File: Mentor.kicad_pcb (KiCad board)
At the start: 2 copper layers, 50 x 100 mm, 41 parts, among them J1 CONN_01X02, J2 CONN_01X06, J3 CONN_01X09, J4 CONN_01X10, J5 CONN_01X02, J6 CONN_01X03, J7 CONN_01X09, Q1 PZT2222A, Q2 PZT2222A, Q3 IRFR3303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

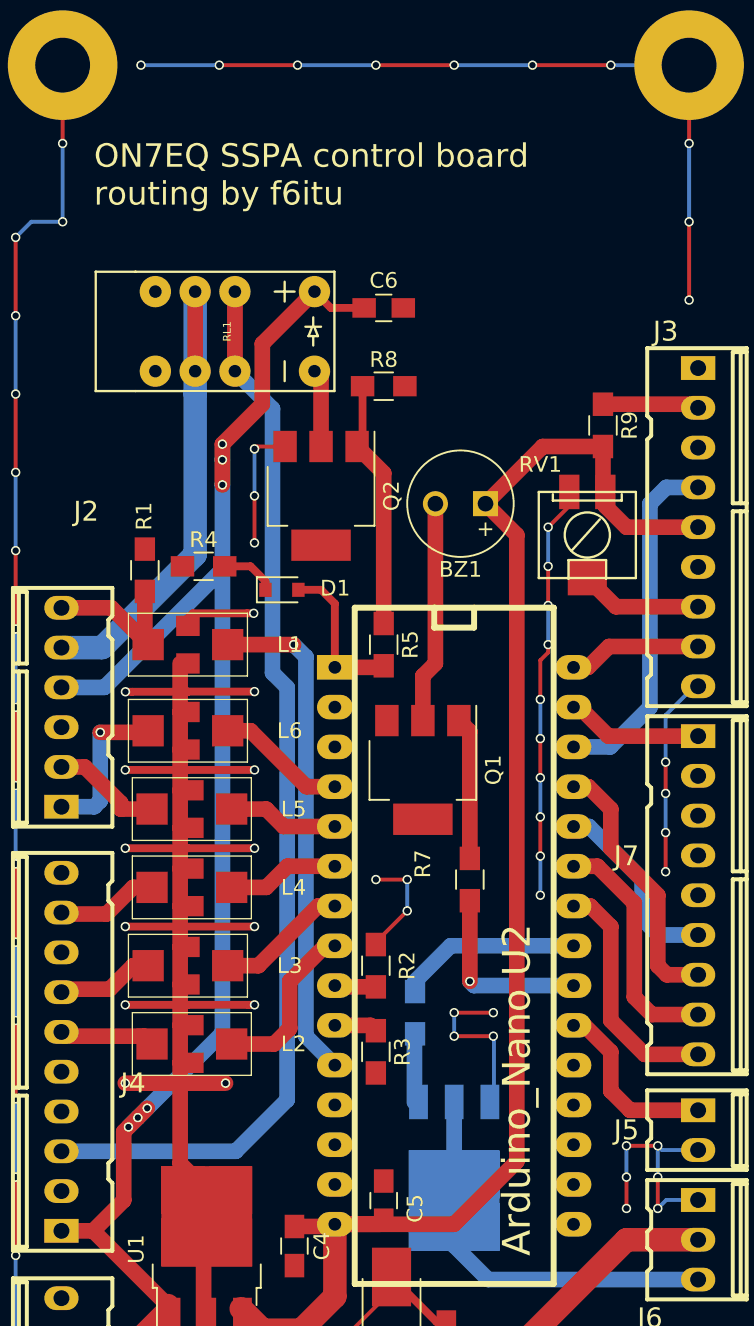
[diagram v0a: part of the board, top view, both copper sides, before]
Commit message: buzzer changed
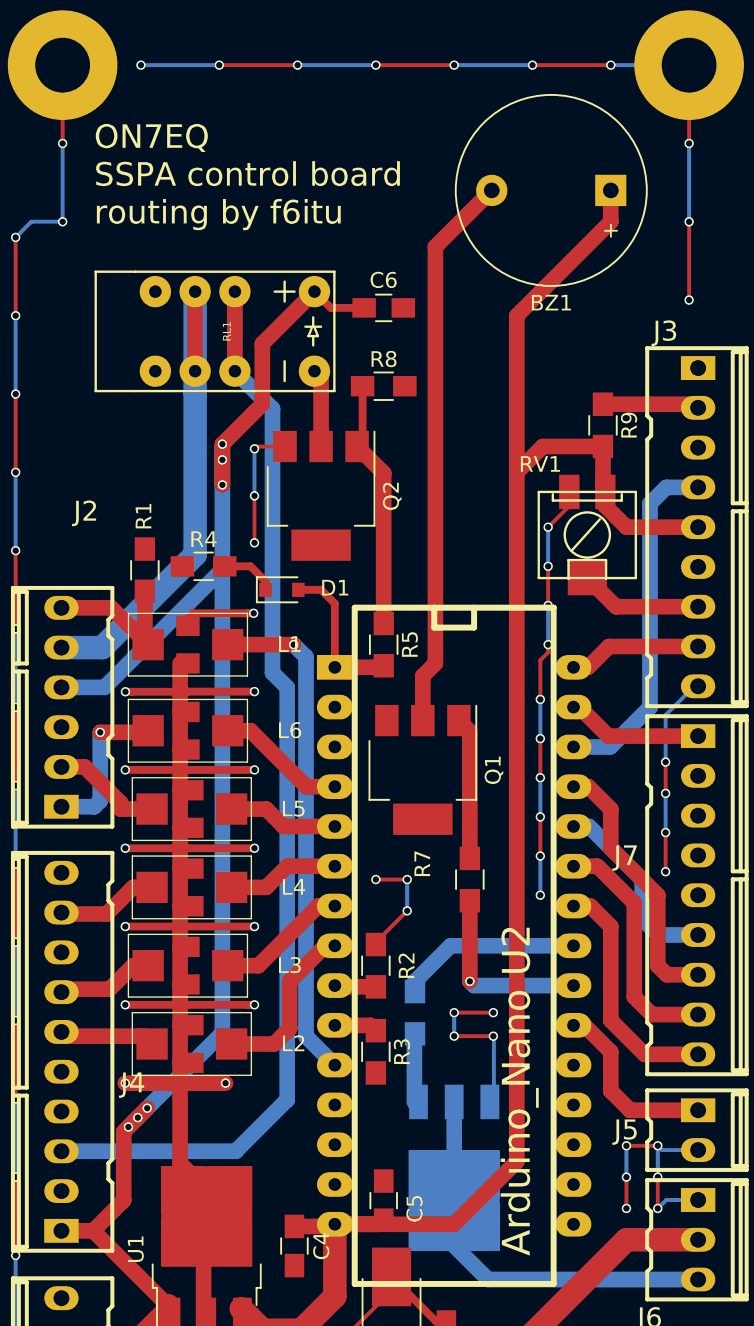
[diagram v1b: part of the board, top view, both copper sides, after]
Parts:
- BZ1: footprint Buzzers_Beepers:MagneticBuzzer_Kingstate_KCG0601 -> Buzzers_Beepers:Buzzer_12x9.5RM7.6
- R4: value R -> 330
- moved BZ1 21.5 mm to (200.0, 48.0)
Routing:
- net Net-(BZ1-Pad2): track 14.2 -> 35.7 mm
- net +5V: track 93.9 -> 112.8 mm
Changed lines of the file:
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@@
     (links 112)
     (no_connects 0)
-    (area 148.5808 34.525 219.0716 135.575)
+    (area 159.924999 34.924999 210.075001 135.075001)
     (thickness 1.6)
     (drawings 13)
-    (tracks 430)
+    (tracks 433)
     (zones 0)
     (modules 41)
@@
   )
   (setup
-    (last_trace_width 0.25)
+    (last_trace_width 1)
     (user_trace_width 0.5)
     (user_trace_width 1)
@@
     )
   )
-  (module Buzzers_Beepers:MagneticBuzzer_Kingstate_KCG0601 (layer F.Cu)
-    (at 192 68 180)
-    (descr "Buzzer, Elektromagnetic Beeper, Summer,")
-    (tags "Kingstate KCG0601 ")
-    (fp_text reference BZ1 (at 1.6 -4.2 180) (layer F.SilkS)
-      (effects (font (size 1 1) (thickness 0.15)))
-    )
-    (fp_text value Buzzer (at 1.6 4.4 180) (layer F.Fab)
-      (effects (font (size 1 1) (thickness 0.15)))
-    )
-    (fp_text user + (at 0 -1.6 180) (layer F.SilkS)
-      (effects (font (size 1 1) (thickness 0.15)))
-    )
-    (fp_text user + (at 0 -1.6 180) (layer F.Fab)
-      (effects (font (size 1 1) (thickness 0.15)))
-    )
-    (fp_circle (center 1.6 0) (end 5.15 0) (layer F.CrtYd) (width 0.05))
-    (fp_circle (center 1.6 0) (end 4.9 0) (layer F.Fab) (width 0.1))
-    (fp_circle (center 1.6 0) (end 2.4 0) (layer F.Fab) (width 0.1))
-    (fp_text user %R (at 1.6 -4.2 180) (layer F.Fab)
-      (effects (font (size 1 1) (thickness 0.15)))
-    )
-    (fp_circle (center 1.6 0) (end 5 0) (layer F.SilkS) (width 0.12))
-    (pad 1 thru_hole rect (at 0 0 180) (size 1.6 1.6) (drill 1) (layers *.Cu *.Mask)
-      (net 1 +5V))
-    (pad 2 thru_hole circle (at 3.2 0 180) (size 1.6 1.6) (drill 1) (layers *.Cu *.Mask)
-      (net 2 "Net-(BZ1-Pad2)"))
-    (model Buzzers_Beepers.3dshapes/MagneticBuzzer_Kingstate_KCG0601.wrl
-      (at (xyz 0.1248031496062992 0 0))
-      (scale (xyz 1 1 1))
-      (rotate (xyz 0 0 180))
-    )
-  )
   (module Capacitors_SMD:C_0805_HandSoldering (layer F.Cu)
     (at 170.8 124.8 180)
@@
       (effects (font (size 1 1) (thickness 0.15)))
     )
-    (fp_text value R (at 0 1.75) (layer F.Fab)
+    (fp_text value 330 (at 0 1.75) (layer F.Fab)
       (effects (font (size 1 1) (thickness 0.15)))
     )
@@
     )
   )
-  (gr_text "ON7EQ SSPA control board\nrouting by f6itu" (at 167 47) (layer F.SilkS)
+  (module Buzzers_Beepers:Buzzer_12x9.5RM7.6 (layer F.Cu)
+    (at 200 48 180)
+    (descr "Generic Buzzer, D12mm height 9.5mm with RM7.6mm")
+    (tags buzzer)
+    (fp_text reference BZ1 (at 3.8 -7.2 180) (layer F.SilkS)
+      (effects (font (size 1 1) (thickness 0.15)))
+    )
+    (fp_text value Buzzer (at 3.8 7.4 180) (layer F.Fab)
+      (effects (font (size 1 1) (thickness 0.15)))
+    )
+    (fp_text user + (at -0.01 -2.54 180) (layer F.Fab)
+      (effects (font (size 1 1) (thickness 0.15)))
+    )
+    (fp_text user + (at -0.01 -2.54 180) (layer F.SilkS)
+      (effects (font (size 1 1) (thickness 0.15)))
+    )
+    (fp_text user %R (at 3.8 -4 180) (layer F.Fab)
+      (effects (font (size 1 1) (thickness 0.15)))
+    )
+    (fp_circle (center 3.8 0) (end 10.05 0) (layer F.CrtYd) (width 0.05))
+    (fp_circle (center 3.8 0) (end 9.8 0) (layer F.Fab) (width 0.1))
+    (fp_circle (center 3.8 0) (end 4.8 0) (layer F.Fab) (width 0.1))
+    (fp_circle (center 3.8 0) (end 9.9 0) (layer F.SilkS) (width 0.12))
+    (pad 1 thru_hole rect (at 0 0 180) (size 2 2) (drill 1) (layers *.Cu *.Mask)
+      (net 1 +5V))
+    (pad 2 thru_hole circle (at 7.6 0 180) (size 2 2) (drill 1) (layers *.Cu *.Mask)
+      (net 2 "Net-(BZ1-Pad2)"))
+    (model ${KISYS3DMOD}/Buzzers_Beepers.3dshapes/Buzzer_12x9.5RM7.6.wrl
+      (at (xyz 0.15 0 0))
+      (scale (xyz 4 4 4))
+      (rotate (xyz 0 0 0))
+    )
+  )
+  (gr_text "ON7EQ \nSSPA control board\nrouting by f6itu" (at 167 47) (layer F.SilkS)
     (effects (font (size 1.5 1.5) (thickness 0.3)) (justify left))
   )
@@
   )
   (gr_line (start 160 135) (end 210 135) (angle 90) (layer Edge.Cuts) (width 0.15))
+  (segment (start 194 66) (end 194 56) (width 1) (layer F.Cu) (net 1))
+  (segment (start 194 56) (end 200 50) (width 1) (layer F.Cu) (net 1))
+  (segment (start 200 50) (end 200 48) (width 1) (layer F.Cu) (net 1))
+  (segment (start 199.5 64.35) (end 195.65 64.35) (width 1) (layer F.Cu) (net 1))
+  (segment (start 195.65 64.35) (end 194 66) (width 1) (layer F.Cu) (net 1))
+  (segment (start 194 66) (end 194 110) (width 1) (layer F.Cu) (net 1))
+  (segment (start 194 110) (end 189.99 114.01) (width 1) (layer F.Cu) (net 1))
+  (segment (start 189.99 114.01) (end 182.38 114.01) (width 1) (layer F.Cu) (net 1))
   (segment (start 176.4 119.4) (end 177.775 120.775) (width 1.5) (layer F.Cu) (net 1))
   (segment (start 177.775 120.775) (end 180.225 120.775) (width 1.5) (layer F.Cu) (net 1))
@@
   (segment (start 179.8 114.15) (end 182.24 114.15) (width 1) (layer F.Cu) (net 1))
   (segment (start 182.24 114.15) (end 182.38 114.01) (width 1) (layer F.Cu) (net 1))
-  (segment (start 199.5 64.35) (end 195.65 64.35) (width 1) (layer F.Cu) (net 1) (status 10))
-  (segment (start 195.65 64.35) (end 192 68) (width 1) (layer F.Cu) (net 1) (status 20))
-  (segment (start 182.38 114.01) (end 189.99 114.01) (width 1) (layer F.Cu) (net 1) (status 10))
-  (segment (start 189.99 114.01) (end 194 110) (width 1) (layer F.Cu) (net 1))
-  (segment (start 194 110) (end 194 70) (width 1) (layer F.Cu) (net 1))
-  (segment (start 194 70) (end 192 68) (width 1) (layer F.Cu) (net 1) (status 20))
   (segment (start 182.38 114.01) (end 185.24 114.01) (width 1) (layer F.Cu) (net 1) (status 30))
   (segment (start 185.24 114.01) (end 185.5 113.75) (width 1) (layer F.Cu) (net 1) (status 30))
@@
   (segment (start 182.24 114.15) (end 182.38 114.01) (width 1) (layer F.Cu) (net 1) (status 30))
   (segment (start 182.14 114.25) (end 182.38 114.01) (width 1) (layer F.Cu) (net 1) (status 30))
-  (segment (start 188 81.85) (end 188 79) (width 1) (layer F.Cu) (net 2) (status 10))
-  (segment (start 188.8 78.2) (end 188.8 68) (width 1) (layer F.Cu) (net 2) (status 20))
+  (segment (start 188 81.85) (end 188 79) (width 1) (layer F.Cu) (net 2))
   (segment (start 188 79) (end 188.8 78.2) (width 1) (layer F.Cu) (net 2))
+  (segment (start 188.8 78.2) (end 188.8 51.6) (width 1) (layer F.Cu) (net 2))
+  (segment (start 188.8 51.6) (end 192.4 48) (width 1) (layer F.Cu) (net 2))
   (segment (start 186 123.625) (end 186 125) (width 0.5) (layer F.Cu) (net 3))
   (segment (start 186 125) (end 186 125.6) (width 0.5) (layer F.Cu) (net 3))

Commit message: minor changes, Gerber and BOM added
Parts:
- C1, C4: moved to B.Cu
- moved C1 10.5 mm to (169.6, 114.4), turned to 0 degrees
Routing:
- net +12V: track 156.1 -> 152.2 mm
- net GND: track 387.9 -> 384.1 mm
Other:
- board text added: "Mentor Μέντωρ ON7EQ SSPA control board routing by f6itu"
- board text removed: "ON7EQ SSPA control board routing by f6itu"

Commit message: Mentor V2 RTM
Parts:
- C6: value C -> 100n
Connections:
- U2 pad 26: LCD04 -> LCD03
- U2 pad 27: LCD03 -> LCD04
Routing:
- net GND: track 384.1 -> 371.5 mm, vias 83 -> 79
- net LCD04: track 12.3 -> 16.3 mm, vias 1 -> 0
- net LCD03: track 17.0 -> 14.2 mm
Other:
- board text added: "Mentor Μέντωρ V2.0 ON7EQ SSPA control board routing by f6itu"
- board text removed: "Mentor Μέντωρ ON7EQ SSPA control board routing by f6itu"
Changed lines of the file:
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@@
     (area 159.924999 34.924999 210.075001 135.075001)
     (thickness 1.6)
-    (drawings 13)
-    (tracks 438)
+    (drawings 14)
+    (tracks 426)
     (zones 0)
     (modules 41)
@@
   )
   (setup
-    (last_trace_width 1)
+    (last_trace_width 0.25)
     (user_trace_width 0.5)
     (user_trace_width 1)
@@
       (net 21 LCD02))
     (pad 26 thru_hole oval (at -8.89 -7.62 270) (size 1.5748 2.286) (drill 0.8128) (layers *.Cu *.Mask F.SilkS)
+      (net 22 LCD03))
+    (pad 27 thru_hole oval (at -11.43 -7.62 270) (size 1.5748 2.286) (drill 0.8128) (layers *.Cu *.Mask F.SilkS)
       (net 24 LCD04))
-    (pad 27 thru_hole oval (at -11.43 -7.62 270) (size 1.5748 2.286) (drill 0.8128) (layers *.Cu *.Mask F.SilkS)
-      (net 22 LCD03))
     (pad 28 thru_hole oval (at -13.97 -7.62 270) (size 1.5748 2.286) (drill 0.8128) (layers *.Cu *.Mask F.SilkS)
       (net 13 LCDE2))
@@
       (effects (font (size 1 1) (thickness 0.15)))
     )
-    (fp_text value C (at 0 1.75) (layer F.Fab)
+    (fp_text value 100n (at 0 1.75) (layer F.Fab)
       (effects (font (size 1 1) (thickness 0.15)))
     )
@@
     )
   )
-  (gr_text "Mentor Μέντωρ \nON7EQ \nSSPA control board\nrouting by f6itu" (at 168 47.8) (layer F.SilkS)
+  (gr_text "Mentor Μέντωρ V2.0\nON7EQ \nSSPA control board\nrouting by f6itu" (at 191 48) (layer B.SilkS)
+    (effects (font (size 1.5 1.5) (thickness 0.3)) (justify left mirror))
+  )
+  (gr_text "Mentor Μέντωρ V2.0\nON7EQ \nSSPA control board\nrouting by f6itu" (at 168 47.8) (layer F.SilkS)
     (effects (font (size 1.5 1.5) (thickness 0.3)) (justify left))
   )
@@
   (segment (start 174 120.775) (end 174 111.625) (width 1) (layer F.Cu) (net 4) (status 30))
   (segment (start 205.5762 79.66) (end 205.34 79.66) (width 0.25) (layer B.Cu) (net 4) (status 30))
-  (segment (start 205.34 79.66) (end 203.5 81.5) (width 0.25) (layer B.Cu) (net 4) (status 10))
-  (segment (start 203.5 81.5) (end 203.5 84.5) (width 0.25) (layer B.Cu) (net 4))
-  (via (at 203.5 84.5) (size 0.6) (drill 0.4) (layers F.Cu B.Cu) (net 4))
-  (segment (start 203.5 84.5) (end 203.5 86.5) (width 0.25) (layer F.Cu) (net 4))
-  (via (at 203.5 86.5) (size 0.6) (drill 0.4) (layers F.Cu B.Cu) (net 4))
-  (segment (start 203.5 86.5) (end 203.5 89) (width 0.25) (layer B.Cu) (net 4))
-  (via (at 203.5 89) (size 0.6) (drill 0.4) (layers F.Cu B.Cu) (net 4))
-  (segment (start 203.5 89) (end 203.5 91.5) (width 0.25) (layer F.Cu) (net 4))
-  (via (at 203.5 91.5) (size 0.6) (drill 0.4) (layers F.Cu B.Cu) (net 4))
   (segment (start 196 77) (end 196 77.5) (width 0.25) (layer F.Cu) (net 4))
   (via (at 196 77) (size 0.6) (drill 0.4) (layers F.Cu B.Cu) (net 4))
@@
   (segment (start 201.5 99.5) (end 201.5 93.5) (width 1) (layer F.Cu) (net 21))
   (segment (start 202.62 100.62) (end 201.5 99.5) (width 1) (layer F.Cu) (net 21))
-  (segment (start 205.5762 98.08) (end 203.58 98.08) (width 1) (layer F.Cu) (net 22) (status 10))
-  (segment (start 200 87.5) (end 198.57 86.07) (width 1) (layer F.Cu) (net 22) (status 20))
-  (segment (start 200 90) (end 200 87.5) (width 1) (layer F.Cu) (net 22))
-  (segment (start 203 93) (end 200 90) (width 1) (layer F.Cu) (net 22))
-  (segment (start 203 97.5) (end 203 93) (width 1) (layer F.Cu) (net 22))
-  (segment (start 203.58 98.08) (end 203 97.5) (width 1) (layer F.Cu) (net 22))
-  (segment (start 198.57 86.07) (end 197.62 86.07) (width 1) (layer F.Cu) (net 22) (status 30))
+  (segment (start 203 91.847) (end 203 95.84035) (width 1) (layer F.Cu) (net 22))
+  (segment (start 203 95.84035) (end 205.23965 98.08) (width 1) (layer F.Cu) (net 22))
+  (segment (start 205.23965 98.08) (end 205.5762 98.08) (width 1) (layer F.Cu) (net 22))
+  (segment (start 197.62 88.61) (end 199.763 88.61) (width 1) (layer F.Cu) (net 22))
+  (segment (start 199.763 88.61) (end 203 91.847) (width 1) (layer F.Cu) (net 22))
   (segment (start 205.5762 103.16) (end 202.16 103.16) (width 1) (layer F.Cu) (net 23) (status 10))
   (segment (start 200 95) (end 198.69 93.69) (width 1) (layer F.Cu) (net 23) (status 20))
@@
   (segment (start 202.16 103.16) (end 200 101) (width 1) (layer F.Cu) (net 23))
   (segment (start 198.69 93.69) (end 197.62 93.69) (width 1) (layer F.Cu) (net 23) (status 30))
-  (segment (start 197.62 88.61) (end 198.61 88.61) (width 1) (layer B.Cu) (net 24) (status 30))
-  (segment (start 198.61 88.61) (end 202 92) (width 1) (layer B.Cu) (net 24) (status 10))
-  (segment (start 203.04 95.54) (end 205.5762 95.54) (width 1) (layer B.Cu) (net 24) (status 20))
+  (segment (start 197.62 86.07) (end 201.07 86.07) (width 1) (layer B.Cu) (net 24))
+  (segment (start 201.07 86.07) (end 202 87) (width 1) (layer B.Cu) (net 24))
+  (segment (start 202 87) (end 202 94.5) (width 1) (layer B.Cu) (net 24))
   (segment (start 202 94.5) (end 203.04 95.54) (width 1) (layer B.Cu) (net 24))
-  (segment (start 202 92) (end 202 94.5) (width 1) (layer B.Cu) (net 24))
-  (via (at 197.62 88.61) (size 0.6) (drill 0.4) (layers F.Cu B.Cu) (net 24) (status 30))
+  (segment (start 203.04 95.54) (end 205.5762 95.54) (width 1) (layer B.Cu) (net 24))
   (segment (start 197.62 80.99) (end 197.99 80.99) (width 1) (layer F.Cu) (net 25) (status 30))
   (segment (start 197.99 80.99) (end 199.84 82.84) (width 1) (layer F.Cu) (net 25) (status 10))
